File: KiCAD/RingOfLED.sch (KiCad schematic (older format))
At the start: 9 parts

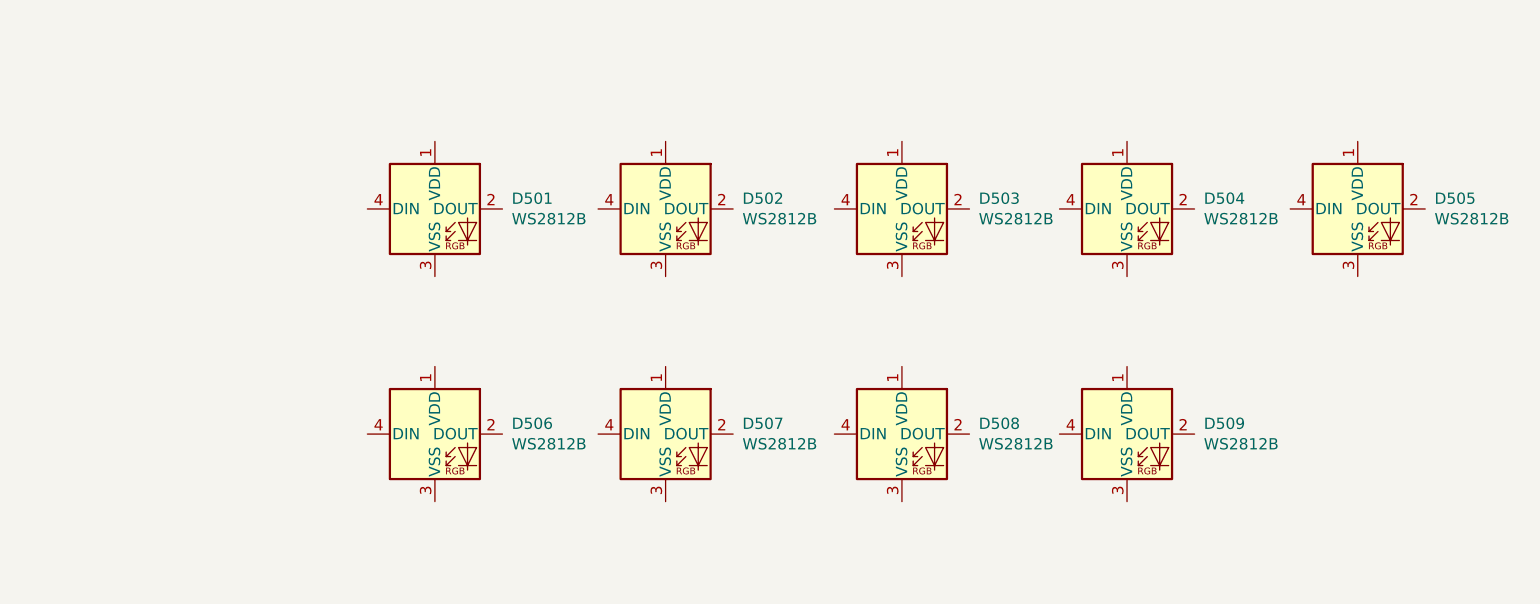
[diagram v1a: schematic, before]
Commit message: Add STM32 base circuit for power control and USB, also a lot of other things
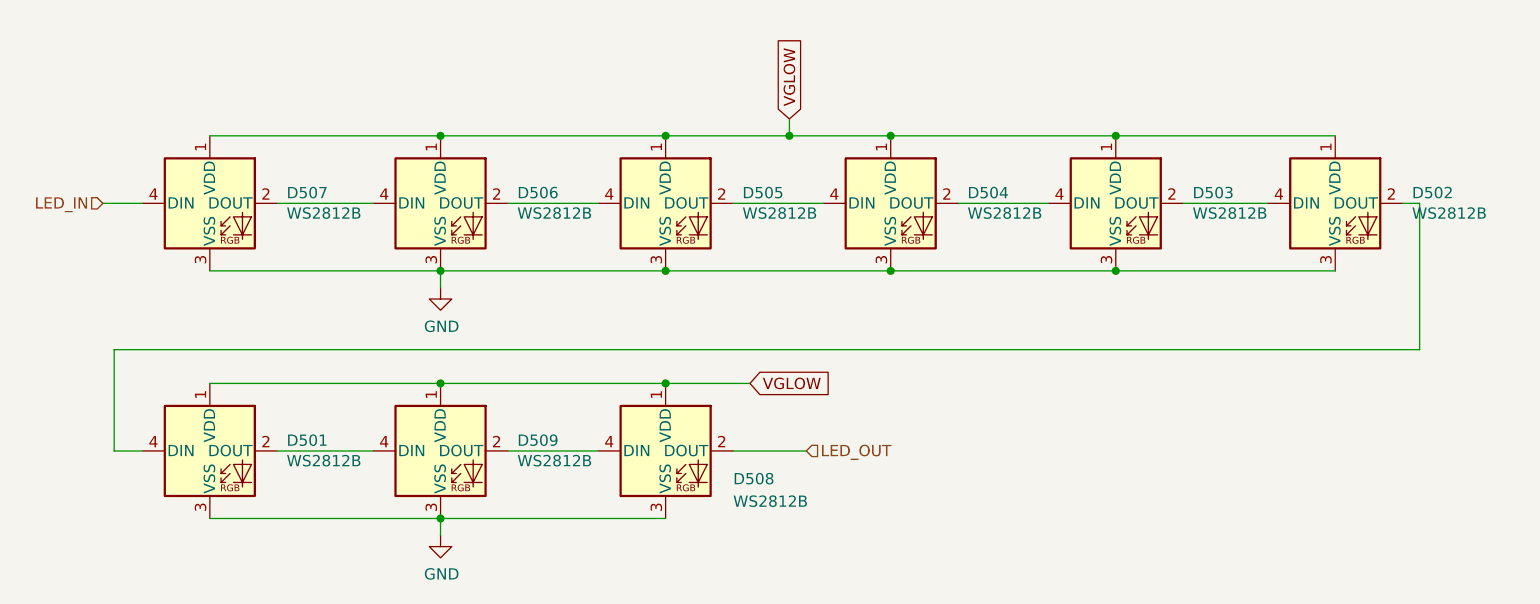
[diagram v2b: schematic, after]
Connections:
- net VGLOW: now reaches D501.1 (VDD)
- net VGLOW: now also D502.1 (VDD), D503.1 (VDD), D504.1 (VDD), D505.1 (VDD), D506.1 (VDD), D507.1 (VDD), D508.1 (VDD), D509.1 (VDD)
- net at D501.2 (DOUT): now also D509.4 (DIN)
- net GND: now reaches D501.3 (VSS)
- net GND: now also D502.3 (VSS), D503.3 (VSS), D504.3 (VSS), D505.3 (VSS), D506.3 (VSS), D507.3 (VSS), D508.3 (VSS), D509.3 (VSS)
- net at D501.4 (DIN): now also D502.2 (DOUT)
- net at D502.4 (DIN): now also D503.2 (DOUT)
- net at D503.4 (DIN): now also D504.2 (DOUT)
- net at D504.4 (DIN): now also D505.2 (DOUT)
- net at D505.4 (DIN): now also D506.2 (DOUT)
- net at D506.4 (DIN): now also D507.2 (DOUT)
- net LED_IN: now reaches D507.4 (DIN)
- net LED_OUT: now reaches D508.2 (DOUT)
- net at D508.4 (DIN): now also D509.2 (DOUT)
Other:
- moved on the sheet: D501, D502, D503, D504, D505, D506, D507, D508, D509
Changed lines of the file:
@@
 $Descr A4 11693 8268
 encoding utf-8
-Sheet 5 7
+Sheet 5 6
 Title ""
 Date ""
@@
 L LED:WS2812B D501
 U 1 1 60F9A2FB
-P 2650 2925
-F 0 "D501" H 2991 2971 50  0000 L CNN
-F 1 "WS2812B" H 2991 2880 50  0000 L CNN
-F 2 "XasPrints:IN-PI42TAS" H 2700 2625 50  0001 L TNN
-F 3 "https://cdn-shop.adafruit.com/datasheets/WS2812B.pdf" H 2750 2550 50  0001 L TNN
-	1    2650 2925
+P 1650 4000
+F 0 "D501" H 1991 4046 50  0000 L CNN
+F 1 "WS2812B" H 1991 3955 50  0000 L CNN
+F 2 "XasPrints:IN-PI42TAS" H 1700 3700 50  0001 L TNN
+F 3 "https://cdn-shop.adafruit.com/datasheets/WS2812B.pdf" H 1750 3625 50  0001 L TNN
+	1    1650 4000
 	1    0    0    -1
 $EndComp
@@
 L LED:WS2812B D502
 U 1 1 60F9AC80
-P 3675 2925
-F 0 "D502" H 4016 2971 50  0000 L CNN
-F 1 "WS2812B" H 4016 2880 50  0000 L CNN
-F 2 "XasPrints:IN-PI42TAS" H 3725 2625 50  0001 L TNN
-F 3 "https://cdn-shop.adafruit.com/datasheets/WS2812B.pdf" H 3775 2550 50  0001 L TNN
-	1    3675 2925
+P 6650 2900
+F 0 "D502" H 6991 2946 50  0000 L CNN
+F 1 "WS2812B" H 6991 2855 50  0000 L CNN
+F 2 "XasPrints:IN-PI42TAS" H 6700 2600 50  0001 L TNN
+F 3 "https://cdn-shop.adafruit.com/datasheets/WS2812B.pdf" H 6750 2525 50  0001 L TNN
+	1    6650 2900
 	1    0    0    -1
 $EndComp
@@
 L LED:WS2812B D503
 U 1 1 60F9B462
-P 4725 2925
-F 0 "D503" H 5066 2971 50  0000 L CNN
-F 1 "WS2812B" H 5066 2880 50  0000 L CNN
-F 2 "XasPrints:IN-PI42TAS" H 4775 2625 50  0001 L TNN
-F 3 "https://cdn-shop.adafruit.com/datasheets/WS2812B.pdf" H 4825 2550 50  0001 L TNN
-	1    4725 2925
+P 5675 2900
+F 0 "D503" H 6016 2946 50  0000 L CNN
+F 1 "WS2812B" H 6016 2855 50  0000 L CNN
+F 2 "XasPrints:IN-PI42TAS" H 5725 2600 50  0001 L TNN
+F 3 "https://cdn-shop.adafruit.com/datasheets/WS2812B.pdf" H 5775 2525 50  0001 L TNN
+	1    5675 2900
 	1    0    0    -1
 $EndComp
@@
 L LED:WS2812B D504
 U 1 1 60F9BB2D
-P 5725 2925
-F 0 "D504" H 6066 2971 50  0000 L CNN
-F 1 "WS2812B" H 6066 2880 50  0000 L CNN
-F 2 "XasPrints:IN-PI42TAS" H 5775 2625 50  0001 L TNN
-F 3 "https://cdn-shop.adafruit.com/datasheets/WS2812B.pdf" H 5825 2550 50  0001 L TNN
-	1    5725 2925
+P 4675 2900
+F 0 "D504" H 5016 2946 50  0000 L CNN
+F 1 "WS2812B" H 5016 2855 50  0000 L CNN
+F 2 "XasPrints:IN-PI42TAS" H 4725 2600 50  0001 L TNN
+F 3 "https://cdn-shop.adafruit.com/datasheets/WS2812B.pdf" H 4775 2525 50  0001 L TNN
+	1    4675 2900
 	1    0    0    -1
 $EndComp
@@
 L LED:WS2812B D505
 U 1 1 60F9BB34
-P 6750 2925
-F 0 "D505" H 7091 2971 50  0000 L CNN
-F 1 "WS2812B" H 7091 2880 50  0000 L CNN
-F 2 "XasPrints:IN-PI42TAS" H 6800 2625 50  0001 L TNN
-F 3 "https://cdn-shop.adafruit.com/datasheets/WS2812B.pdf" H 6850 2550 50  0001 L TNN
-	1    6750 2925
+P 3675 2900
+F 0 "D505" H 4016 2946 50  0000 L CNN
+F 1 "WS2812B" H 4016 2855 50  0000 L CNN
+F 2 "XasPrints:IN-PI42TAS" H 3725 2600 50  0001 L TNN
+F 3 "https://cdn-shop.adafruit.com/datasheets/WS2812B.pdf" H 3775 2525 50  0001 L TNN
+	1    3675 2900
 	1    0    0    -1
 $EndComp
@@
 L LED:WS2812B D506
 U 1 1 60F9BE8A
-P 2650 3925
-F 0 "D506" H 2991 3971 50  0000 L CNN
-F 1 "WS2812B" H 2991 3880 50  0000 L CNN
-F 2 "XasPrints:IN-PI42TAS" H 2700 3625 50  0001 L TNN
-F 3 "https://cdn-shop.adafruit.com/datasheets/WS2812B.pdf" H 2750 3550 50  0001 L TNN
-	1    2650 3925
+P 2675 2900
+F 0 "D506" H 3016 2946 50  0000 L CNN
+F 1 "WS2812B" H 3016 2855 50  0000 L CNN
+F 2 "XasPrints:IN-PI42TAS" H 2725 2600 50  0001 L TNN
+F 3 "https://cdn-shop.adafruit.com/datasheets/WS2812B.pdf" H 2775 2525 50  0001 L TNN
+	1    2675 2900
 	1    0    0    -1
 $EndComp
@@
 L LED:WS2812B D507
 U 1 1 60F9BE91
-P 3675 3925
-F 0 "D507" H 4016 3971 50  0000 L CNN
-F 1 "WS2812B" H 4016 3880 50  0000 L CNN
-F 2 "XasPrints:IN-PI42TAS" H 3725 3625 50  0001 L TNN
-F 3 "https://cdn-shop.adafruit.com/datasheets/WS2812B.pdf" H 3775 3550 50  0001 L TNN
-	1    3675 3925
+P 1650 2900
+F 0 "D507" H 1991 2946 50  0000 L CNN
+F 1 "WS2812B" H 1991 2855 50  0000 L CNN
+F 2 "XasPrints:IN-PI42TAS" H 1700 2600 50  0001 L TNN
+F 3 "https://cdn-shop.adafruit.com/datasheets/WS2812B.pdf" H 1750 2525 50  0001 L TNN
+	1    1650 2900
 	1    0    0    -1
 $EndComp
@@
 L LED:WS2812B D508
 U 1 1 60F9BE98
-P 4725 3925
-F 0 "D508" H 5066 3971 50  0000 L CNN
-F 1 "WS2812B" H 5066 3880 50  0000 L CNN
-F 2 "XasPrints:IN-PI42TAS" H 4775 3625 50  0001 L TNN
-F 3 "https://cdn-shop.adafruit.com/datasheets/WS2812B.pdf" H 4825 3550 50  0001 L TNN
-	1    4725 3925
+P 3675 4000
+F 0 "D508" H 3975 3875 50  0000 L CNN
+F 1 "WS2812B" H 3975 3775 50  0000 L CNN
+F 2 "XasPrints:IN-PI42TAS" H 3725 3700 50  0001 L TNN
+F 3 "https://cdn-shop.adafruit.com/datasheets/WS2812B.pdf" H 3775 3625 50  0001 L TNN
+	1    3675 4000
 	1    0    0    -1
 $EndComp
@@
 L LED:WS2812B D509
 U 1 1 60F9BE9F
-P 5725 3925
-F 0 "D509" H 6066 3971 50  0000 L CNN
-F 1 "WS2812B" H 6066 3880 50  0000 L CNN
-F 2 "XasPrints:IN-PI42TAS" H 5775 3625 50  0001 L TNN
-F 3 "https://cdn-shop.adafruit.com/datasheets/WS2812B.pdf" H 5825 3550 50  0001 L TNN
-	1    5725 3925
-	1    0    0    -1
-$EndComp
+P 2675 4000
+F 0 "D509" H 3016 4046 50  0000 L CNN
+F 1 "WS2812B" H 3016 3955 50  0000 L CNN
+F 2 "XasPrints:IN-PI42TAS" H 2725 3700 50  0001 L TNN
+F 3 "https://cdn-shop.adafruit.com/datasheets/WS2812B.pdf" H 2775 3625 50  0001 L TNN
+	1    2675 4000
+	1    0    0    -1
+$EndComp
+Wire Wire Line
+	1950 2900 2375 2900
+Wire Wire Line
+	2975 2900 3375 2900
+Wire Wire Line
+	3975 2900 4375 2900
+Wire Wire Line
+	4975 2900 5375 2900
+Wire Wire Line
+	5975 2900 6350 2900
+Wire Wire Line
+	1650 3200 2675 3200
+Connection ~ 2675 3200
+Wire Wire Line
+	2675 3200 3675 3200
+Connection ~ 3675 3200
+Wire Wire Line
+	3675 3200 4675 3200
+Connection ~ 4675 3200
+Wire Wire Line
+	4675 3200 5675 3200
+Connection ~ 5675 3200
+Wire Wire Line
+	5675 3200 6650 3200
+Wire Wire Line
+	6650 2600 5675 2600
+Connection ~ 2675 2600
+Wire Wire Line
+	2675 2600 1650 2600
+Connection ~ 3675 2600
+Wire Wire Line
+	3675 2600 2675 2600
+Connection ~ 4675 2600
+Wire Wire Line
+	4675 2600 4225 2600
+Connection ~ 5675 2600
+Wire Wire Line
+	5675 2600 4675 2600
+Wire Wire Line
+	1650 4300 2675 4300
+Connection ~ 2675 4300
+Wire Wire Line
+	2675 4300 3675 4300
+Wire Wire Line
+	3675 3700 2675 3700
+Connection ~ 2675 3700
+Wire Wire Line
+	2675 3700 1650 3700
+$Comp
+L power:GND #PWR0150
+U 1 1 611235B5
+P 2675 4375
+F 0 "#PWR0150" H 2675 4125 50  0001 C CNN
+F 1 "GND" H 2680 4202 50  0000 C CNN
+F 2 "" H 2675 4375 50  0001 C CNN
+F 3 "" H 2675 4375 50  0001 C CNN
+	1    2675 4375
+	1    0    0    -1
+$EndComp
+Wire Wire Line
+	2675 4375 2675 4300
+$Comp
+L power:GND #PWR0151
+U 1 1 61123991
+P 2675 3275
+F 0 "#PWR0151" H 2675 3025 50  0001 C CNN
+F 1 "GND" H 2680 3102 50  0000 C CNN
+F 2 "" H 2675 3275 50  0001 C CNN
+F 3 "" H 2675 3275 50  0001 C CNN
+	1    2675 3275
+	1    0    0    -1
+$EndComp
+Wire Wire Line
+	2675 3275 2675 3200
+Wire Wire Line
+	1950 4000 2375 4000
+Wire Wire Line
+	2975 4000 3375 4000
+Wire Wire Line
+	6950 2900 7025 2900
+Wire Wire Line
+	7025 2900 7025 3550
+Wire Wire Line
+	7025 3550 1225 3550
+Wire Wire Line
+	1225 3550 1225 4000
+Wire Wire Line
+	1225 4000 1350 4000
+Text GLabel 4225 2525 1    50   Input ~ 0
+VGLOW
+Wire Wire Line
+	4225 2525 4225 2600
+Connection ~ 4225 2600
+Wire Wire Line
+	4225 2600 3675 2600
+Text GLabel 4050 3700 2    50   Input ~ 0
+VGLOW
+Wire Wire Line
+	4050 3700 3675 3700
+Connection ~ 3675 3700
+Text HLabel 1175 2900 0    50   Input ~ 0
+LED_IN
+Wire Wire Line
+	1175 2900 1350 2900
+Text HLabel 4300 4000 2    50   Input ~ 0
+LED_OUT
+Wire Wire Line
+	4300 4000 3975 4000
 $EndSCHEMATC

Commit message: Finalize PCB schematics
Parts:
- added C608: 0.1uF 0402, Capacitor_SMD:C_0402_1005Metric, symbol Device:C_Small
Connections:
- net GND: now also C608.2
- net VGLOW: now also C608.1
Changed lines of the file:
@@
 Connection ~ 4675 2600
 Wire Wire Line
-	4675 2600 4225 2600
+	4675 2600 4550 2600
 Connection ~ 5675 2600
 Wire Wire Line
@@
 Wire Wire Line
 	4300 4000 3975 4000
+$Comp
+L Device:C_Small C?
+U 1 1 6145291E
+P 4550 2425
+AR Path="/60EDF44C/6145291E" Ref="C?"  Part="1"
+AR Path="/60F2BC2A/6145291E" Ref="C?"  Part="1"
+AR Path="/60F9A292/6145291E" Ref="C608"  Part="1"
+F 0 "C608" H 4642 2471 50  0000 L CNN
+F 1 "0.1uF 0402" H 4050 2350 50  0000 L CNN
+F 2 "Capacitor_SMD:C_0402_1005Metric" H 4550 2425 50  0001 C CNN
+F 3 "~" H 4550 2425 50  0001 C CNN
+	1    4550 2425
+	-1   0    0    1
+$EndComp
+$Comp
+L power:GND #PWR0165
+U 1 1 61453066
+P 4550 2300
+F 0 "#PWR0165" H 4550 2050 50  0001 C CNN
+F 1 "GND" H 4555 2127 50  0000 C CNN
+F 2 "" H 4550 2300 50  0001 C CNN
+F 3 "" H 4550 2300 50  0001 C CNN
+	1    4550 2300
+	-1   0    0    1
+$EndComp
+Wire Wire Line
+	4550 2325 4550 2300
+Wire Wire Line
+	4550 2525 4550 2600
+Connection ~ 4550 2600
+Wire Wire Line
+	4550 2600 4225 2600
 $EndSCHEMATC
